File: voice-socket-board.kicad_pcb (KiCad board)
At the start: 2 copper layers, 150 x 100 mm, 280 parts, among them J1 JACK_MONO_SW, J2 JACK_MONO_SW, J3 JACK_MONO_SW, P1 CONN_01X03, P2 CONN_01X03, P3 CONN_02X05, P4 DDR3-DIMM, Q1 MMBT3904, Q10 2N3906, Q2 DMMT3904W, Q3 2N7002, Q4 2N7002, Q5 MMBT3904, Q6 2N3906, Q7 MMBT3904, Q8 MMBT3904, Q9 MMBT3904, SW1 SPST, SW10 SP3T, SW11 SP3T, SW12 SP3T, SW13 SP3T, SW14 SPST, SW15 TACT_SWITCH, SW2 SPST, SW3 SP3T, SW4 SP3T, SW5 SPST, SW6 SPST, SW7 Switch_SPDT_x2, SW8 2P3T, SW9 SP3T, U1 LM833, U10 TL072-, U11 NE5534, U2 TL072-, U3 TL072-, U4 TL072-, U5 TL072-, U6 TL072-, U7 MAX9945, U8 CD4013, U9 TL072-

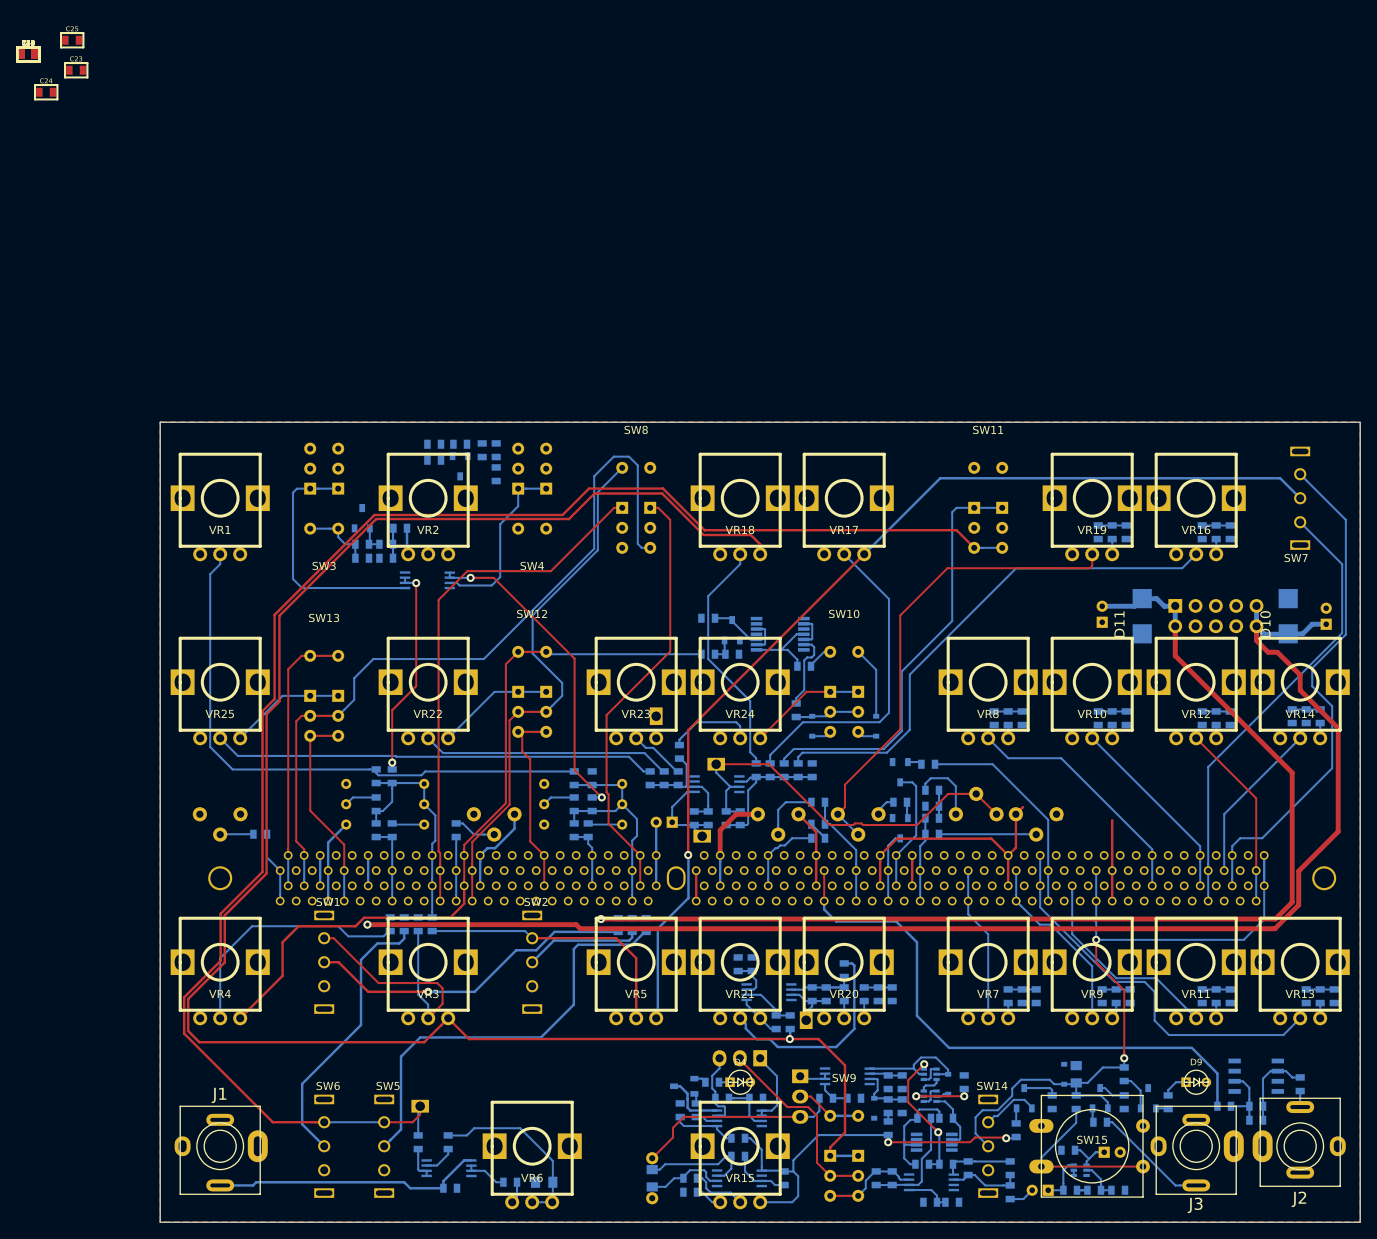
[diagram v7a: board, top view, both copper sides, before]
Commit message: all non power and gnd traces routed
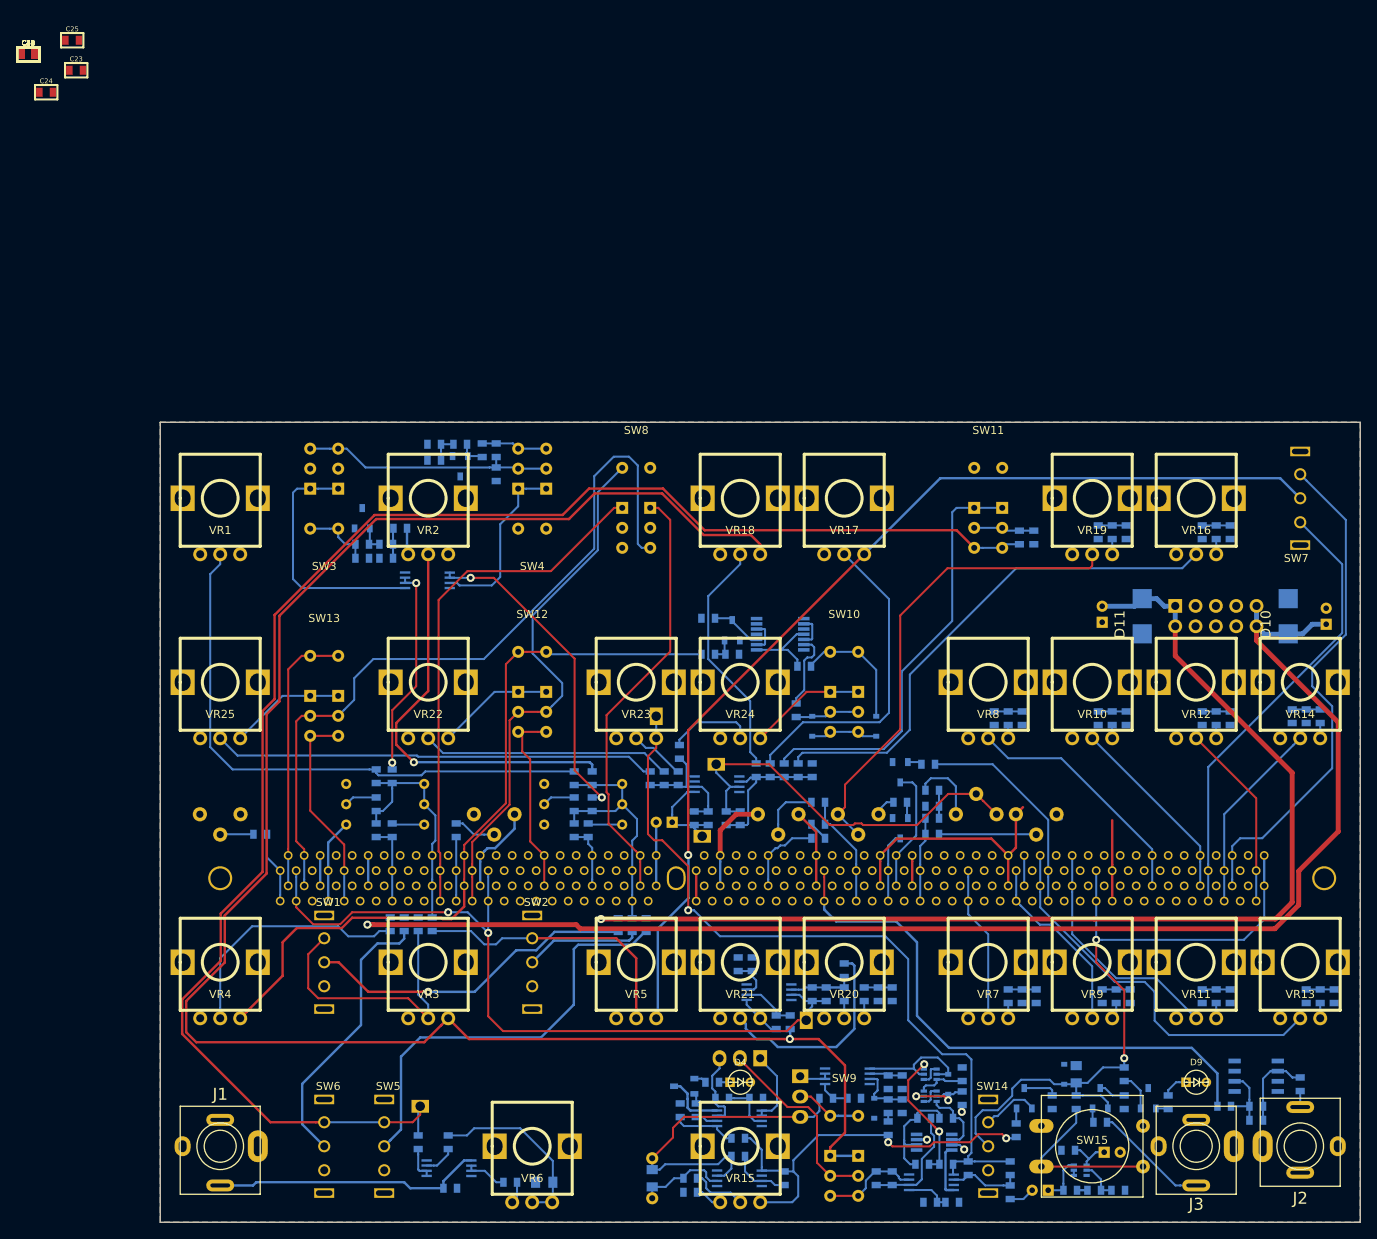
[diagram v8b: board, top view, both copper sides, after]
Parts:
- R71, R93, R94: moved to B.Cu
- moved R71 172.9 mm to (145.2, 121.5), turned to 90 degrees
- moved R94 139.5 mm to (154.2, 54.4), turned to 90 degrees
- moved R93 137.8 mm to (152.4, 54.4), turned to 270 degrees
- moved R72 2.02 mm to (145.2, 124.5), turned to 90 degrees
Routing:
- net VCO1_PWM_CV: track 7.39 -> 97.8 mm, vias 0 -> 2
- net NOISE: track 8.63 -> 96.5 mm, vias 0 -> 1
- net VCO2_TUNE: track 0.00 -> 51.8 mm, vias 0 -> 1
- net Net-(R25-Pad2): track 0.00 -> 31.8 mm
- net Net-(R24-Pad2): track 0.00 -> 8.27 mm
- net Net-(R93-Pad1): track 0.00 -> 7.59 mm
- net -12V: track 182.4 -> 189.0 mm
- net VCO2_PITCH_CV: track 29.6 -> 35.3 mm
- net EG2_RELEASE_CV: track 20.5 -> 24.3 mm
- net EG1_SUSTAIN_CV: track 25.9 -> 29.7 mm
- net EG1_INV_OUT: track 0.00 -> 3.80 mm
- net Net-(C4-Pad1): track 0.00 -> 3.55 mm
- net Net-(D7-Pad1): track 12.2 -> 15.7 mm
- net Net-(D6-Pad2): track 4.95 -> 8.45 mm
- net Net-(D2-Pad1): track 0.00 -> 3.37 mm
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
